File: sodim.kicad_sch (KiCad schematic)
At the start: 7 parts, among them J1 Edge_Conn_Bus_DDR5_SODIMM_1xD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, U7 AT24CS01_SOT23

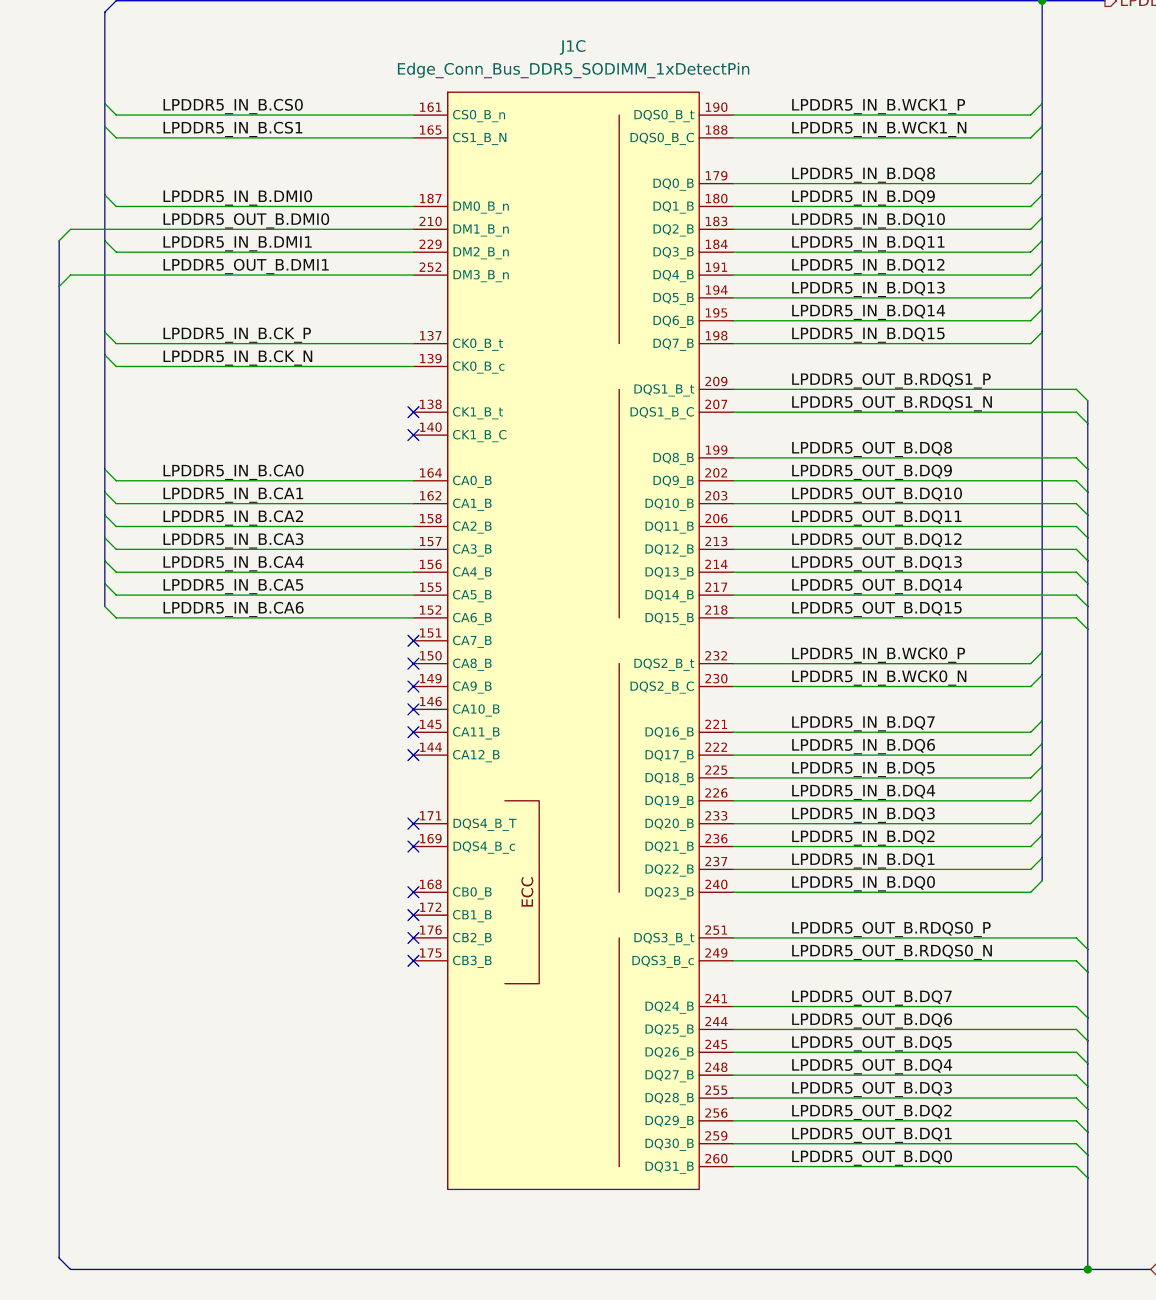
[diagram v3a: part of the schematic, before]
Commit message: [#52835] schematics: swap pins within groups
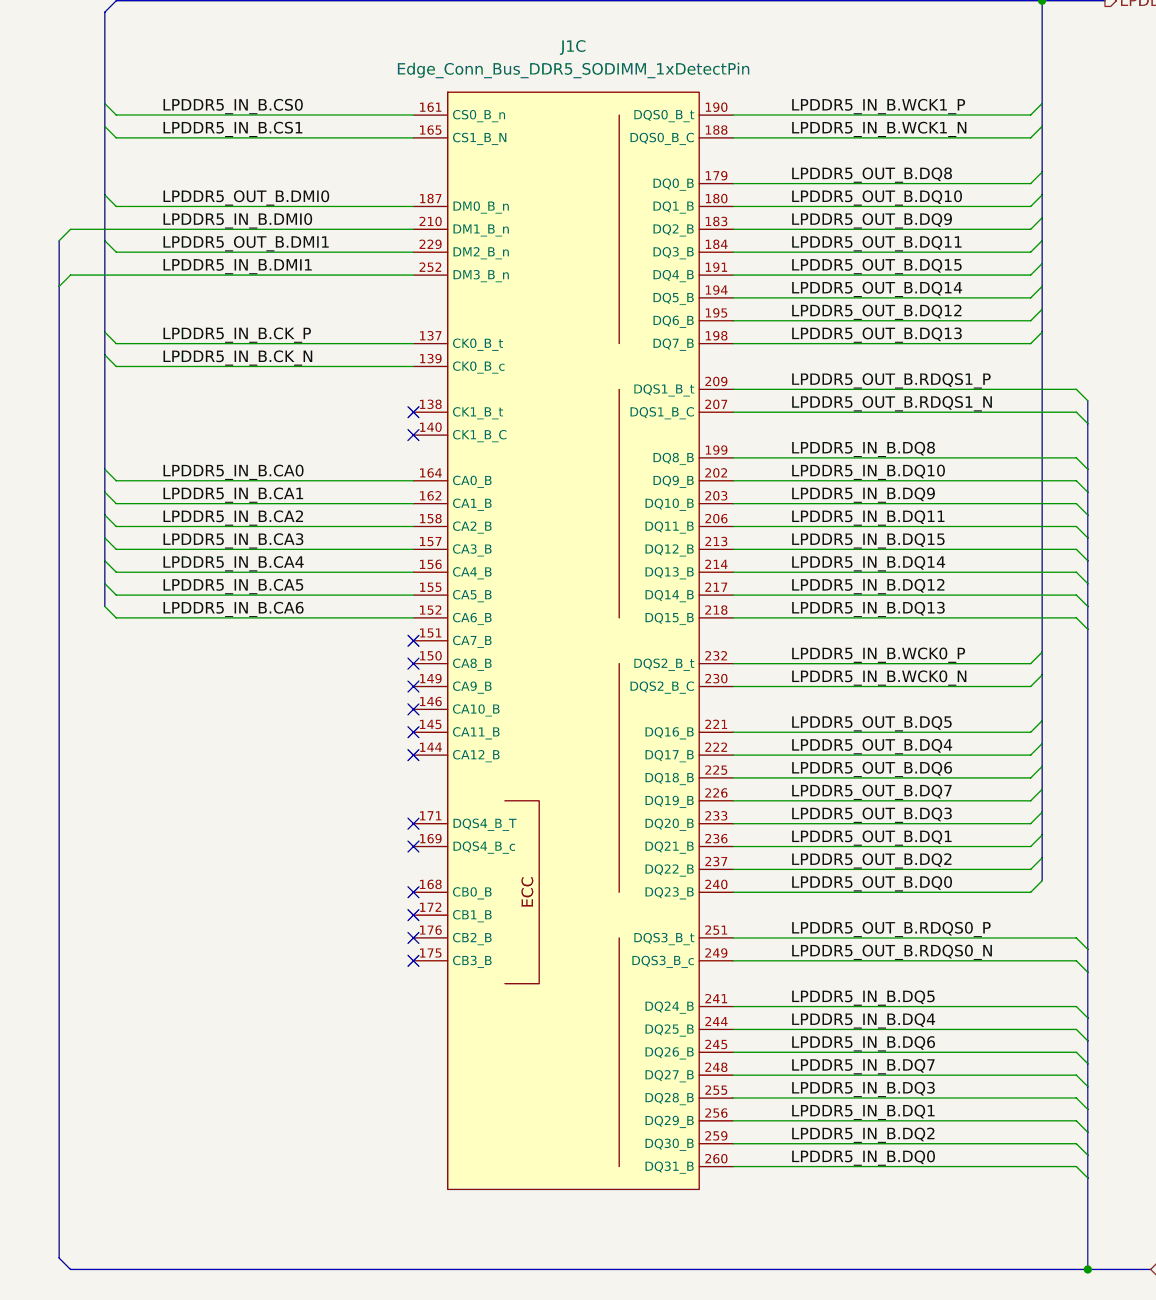
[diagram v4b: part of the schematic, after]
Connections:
- net LPDDR5_IN_B.DMI0: now also J1.210 (DM1_B_n); no longer J1.187 (DM0_B_n)
- net LPDDR5_IN_B.DMI1: now also J1.252 (DM3_B_n); no longer J1.229 (DM2_B_n)
- net LPDDR5_IN_B.DQ0: now also J1.260 (DQ31_B); no longer J1.240 (DQ23_B)
- net LPDDR5_IN_B.DQ1: now also J1.256 (DQ29_B); no longer J1.237 (DQ22_B)
- net LPDDR5_IN_B.DQ10: now also J1.202 (DQ9_B); no longer J1.183 (DQ2_B)
- net LPDDR5_IN_B.DQ11: now also J1.206 (DQ11_B); no longer J1.184 (DQ3_B)
- net LPDDR5_IN_B.DQ12: now also J1.217 (DQ14_B); no longer J1.191 (DQ4_B)
- net LPDDR5_IN_B.DQ13: now also J1.218 (DQ15_B); no longer J1.194 (DQ5_B)
- net LPDDR5_IN_B.DQ14: now also J1.214 (DQ13_B); no longer J1.195 (DQ6_B)
- net LPDDR5_IN_B.DQ15: now also J1.213 (DQ12_B); no longer J1.198 (DQ7_B)
- net LPDDR5_IN_B.DQ2: now also J1.259 (DQ30_B); no longer J1.236 (DQ21_B)
- net LPDDR5_IN_B.DQ3: now also J1.255 (DQ28_B); no longer J1.233 (DQ20_B)
- net LPDDR5_IN_B.DQ4: now also J1.244 (DQ25_B); no longer J1.226 (DQ19_B)
- net LPDDR5_IN_B.DQ5: now also J1.241 (DQ24_B); no longer J1.225 (DQ18_B)
- net LPDDR5_IN_B.DQ6: now also J1.245 (DQ26_B); no longer J1.222 (DQ17_B)
- net LPDDR5_IN_B.DQ7: now also J1.248 (DQ27_B); no longer J1.221 (DQ16_B)
- net LPDDR5_IN_B.DQ8: now also J1.199 (DQ8_B); no longer J1.179 (DQ0_B)
- net LPDDR5_IN_B.DQ9: now also J1.203 (DQ10_B); no longer J1.180 (DQ1_B)
- net LPDDR5_OUT_B.DMI0: now also J1.187 (DM0_B_n); no longer J1.210 (DM1_B_n)
- net LPDDR5_OUT_B.DMI1: now also J1.229 (DM2_B_n); no longer J1.252 (DM3_B_n)
- net LPDDR5_OUT_B.DQ0: now also J1.240 (DQ23_B); no longer J1.260 (DQ31_B)
- net LPDDR5_OUT_B.DQ1: now also J1.236 (DQ21_B); no longer J1.259 (DQ30_B)
- net LPDDR5_OUT_B.DQ10: now also J1.180 (DQ1_B); no longer J1.203 (DQ10_B)
- net LPDDR5_OUT_B.DQ11: now also J1.184 (DQ3_B); no longer J1.206 (DQ11_B)
- net LPDDR5_OUT_B.DQ12: now also J1.195 (DQ6_B); no longer J1.213 (DQ12_B)
- net LPDDR5_OUT_B.DQ13: now also J1.198 (DQ7_B); no longer J1.214 (DQ13_B)
- net LPDDR5_OUT_B.DQ14: now also J1.194 (DQ5_B); no longer J1.217 (DQ14_B)
- net LPDDR5_OUT_B.DQ15: now also J1.191 (DQ4_B); no longer J1.218 (DQ15_B)
- net LPDDR5_OUT_B.DQ2: now also J1.237 (DQ22_B); no longer J1.256 (DQ29_B)
- net LPDDR5_OUT_B.DQ3: now also J1.233 (DQ20_B); no longer J1.255 (DQ28_B)
- net LPDDR5_OUT_B.DQ4: now also J1.222 (DQ17_B); no longer J1.248 (DQ27_B)
- net LPDDR5_OUT_B.DQ5: now also J1.221 (DQ16_B); no longer J1.245 (DQ26_B)
- net LPDDR5_OUT_B.DQ6: now also J1.225 (DQ18_B); no longer J1.244 (DQ25_B)
- net LPDDR5_OUT_B.DQ7: now also J1.226 (DQ19_B); no longer J1.241 (DQ24_B)
- net LPDDR5_OUT_B.DQ8: now also J1.179 (DQ0_B); no longer J1.199 (DQ8_B)
- net LPDDR5_OUT_B.DQ9: now also J1.183 (DQ2_B); no longer J1.202 (DQ9_B)
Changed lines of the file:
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@@
     (effects (font (size 1.27 1.27)) (justify left bottom))
   )
-  (label "LPDDR5_IN_B.DQ3" (at 279.4 182.88 0)
+  (label "LPDDR5_IN_B.DQ3" (at 279.4 213.36 0)
     (effects (font (size 1.27 1.27)) (justify left bottom))
   )
@@
     (effects (font (size 1.27 1.27)) (justify left bottom))
   )
-  (label "LPDDR5_OUT_B.DQ3" (at 279.4 213.36 0)
-    (effects (font (size 1.27 1.27)) (justify left bottom))
-  )
-  (label "LPDDR5_OUT_B.DQ6" (at 279.4 205.74 0)
+  (label "LPDDR5_OUT_B.DQ3" (at 279.4 182.88 0)
+    (effects (font (size 1.27 1.27)) (justify left bottom))
+  )
+  (label "LPDDR5_OUT_B.DQ6" (at 279.4 177.8 0)
     (effects (font (size 1.27 1.27)) (justify left bottom))
   )
@@
     (effects (font (size 1.27 1.27)) (justify left bottom))
   )
-  (label "LPDDR5_IN_B.DQ6" (at 279.4 175.26 0)
+  (label "LPDDR5_IN_B.DQ6" (at 279.4 208.28 0)
     (effects (font (size 1.27 1.27)) (justify left bottom))
   )
@@
     (effects (font (size 1.27 1.27)) (justify left bottom))
   )
-  (label "LPDDR5_IN_B.DMI0" (at 209.55 114.3 0)
-    (effects (font (size 1.27 1.27)) (justify left bottom))
-  )
-  (label "LPDDR5_OUT_B.DQ9" (at 279.4 144.78 0)
+  (label "LPDDR5_IN_B.DMI0" (at 209.55 116.84 0)
+    (effects (font (size 1.27 1.27)) (justify left bottom))
+  )
+  (label "LPDDR5_OUT_B.DQ9" (at 279.4 116.84 0)
     (effects (font (size 1.27 1.27)) (justify left bottom))
   )
@@
     (effects (font (size 1.27 1.27)) (justify left bottom))
   )
-  (label "LPDDR5_IN_B.DQ15" (at 279.4 129.54 0)
+  (label "LPDDR5_IN_B.DQ15" (at 279.4 152.4 0)
     (effects (font (size 1.27 1.27)) (justify left bottom))
   )
@@
     (effects (font (size 1.27 1.27)) (justify left bottom))
   )
-  (label "LPDDR5_OUT_B.DQ14" (at 279.4 157.48 0)
+  (label "LPDDR5_OUT_B.DQ14" (at 279.4 124.46 0)
     (effects (font (size 1.27 1.27)) (justify left bottom))
   )
@@
     (effects (font (size 1.27 1.27)) (justify left bottom))
   )
-  (label "LPDDR5_OUT_B.DQ13" (at 279.4 154.94 0)
-    (effects (font (size 1.27 1.27)) (justify left bottom))
-  )
-  (label "LPDDR5_OUT_B.DQ11" (at 279.4 149.86 0)
-    (effects (font (size 1.27 1.27)) (justify left bottom))
-  )
-  (label "LPDDR5_IN_B.DQ7" (at 279.4 172.72 0)
+  (label "LPDDR5_OUT_B.DQ13" (at 279.4 129.54 0)
+    (effects (font (size 1.27 1.27)) (justify left bottom))
+  )
+  (label "LPDDR5_OUT_B.DQ11" (at 279.4 119.38 0)
+    (effects (font (size 1.27 1.27)) (justify left bottom))
+  )
+  (label "LPDDR5_IN_B.DQ7" (at 279.4 210.82 0)
     (effects (font (size 1.27 1.27)) (justify left bottom))
   )
@@
     (effects (font (size 1.27 1.27)) (justify left bottom))
   )
-  (label "LPDDR5_OUT_B.DMI0" (at 209.55 116.84 0)
-    (effects (font (size 1.27 1.27)) (justify left bottom))
-  )
-  (label "LPDDR5_OUT_B.DQ5" (at 279.4 208.28 0)
+  (label "LPDDR5_OUT_B.DMI0" (at 209.55 114.3 0)
+    (effects (font (size 1.27 1.27)) (justify left bottom))
+  )
+  (label "LPDDR5_OUT_B.DQ5" (at 279.4 172.72 0)
     (effects (font (size 1.27 1.27)) (justify left bottom))
   )
@@
     (effects (font (size 1.27 1.27)) (justify left bottom))
   )
-  (label "LPDDR5_IN_B.DQ5" (at 279.4 177.8 0)
+  (label "LPDDR5_IN_B.DQ5" (at 279.4 203.2 0)
     (effects (font (size 1.27 1.27)) (justify left bottom))
   )
@@
     (effects (font (size 1.27 1.27)) (justify left bottom))
   )
-  (label "LPDDR5_OUT_B.DQ8" (at 279.4 142.24 0)
+  (label "LPDDR5_OUT_B.DQ8" (at 279.4 111.76 0)
     (effects (font (size 1.27 1.27)) (justify left bottom))
   )
@@
     (effects (font (size 1.27 1.27)) (justify left bottom))
   )
-  (label "LPDDR5_OUT_B.DQ10" (at 279.4 147.32 0)
+  (label "LPDDR5_OUT_B.DQ10" (at 279.4 114.3 0)
     (effects (font (size 1.27 1.27)) (justify left bottom))
   )
@@
     (effects (font (size 1.27 1.27)) (justify left bottom))
   )
-  (label "LPDDR5_OUT_B.DQ12" (at 279.4 152.4 0)
+  (label "LPDDR5_OUT_B.DQ12" (at 279.4 127 0)
     (effects (font (size 1.27 1.27)) (justify left bottom))
   )
@@
     (effects (font (size 1.27 1.27)) (justify left bottom))
   )
-  (label "LPDDR5_IN_B.DQ8" (at 279.4 111.76 0)
+  (label "LPDDR5_IN_B.DQ8" (at 279.4 142.24 0)
     (effects (font (size 1.27 1.27)) (justify left bottom))
   )
@@
     (effects (font (size 1.27 1.27)) (justify left bottom))
   )
-  (label "LPDDR5_OUT_B.DQ1" (at 279.4 218.44 0)
-    (effects (font (size 1.27 1.27)) (justify left bottom))
-  )
-  (label "LPDDR5_IN_B.DMI1" (at 209.55 119.38 0)
+  (label "LPDDR5_OUT_B.DQ1" (at 279.4 185.42 0)
+    (effects (font (size 1.27 1.27)) (justify left bottom))
+  )
+  (label "LPDDR5_IN_B.DMI1" (at 209.55 121.92 0)
     (effects (font (size 1.27 1.27)) (justify left bottom))
   )
@@
     (effects (font (size 1.27 1.27)) (justify left bottom))
   )
-  (label "LPDDR5_OUT_B.DMI1" (at 209.55 121.92 0)
+  (label "LPDDR5_OUT_B.DMI1" (at 209.55 119.38 0)
     (effects (font (size 1.27 1.27)) (justify left bottom))
   )
@@
     (effects (font (size 1.27 1.27)) (justify left bottom))
   )
-  (label "LPDDR5_IN_B.DQ4" (at 279.4 180.34 0)
+  (label "LPDDR5_IN_B.DQ4" (at 279.4 205.74 0)
     (effects (font (size 1.27 1.27)) (justify left bottom))
   )
@@
     (effects (font (size 1.27 1.27)) (justify left bottom))
   )
-  (label "LPDDR5_IN_B.DQ9" (at 279.4 114.3 0)
+  (label "LPDDR5_IN_B.DQ9" (at 279.4 147.32 0)
     (effects (font (size 1.27 1.27)) (justify left bottom))
   )
@@
     (effects (font (size 1.27 1.27)) (justify left bottom))
   )
-  (label "LPDDR5_OUT_B.DQ0" (at 279.4 220.98 0)
-    (effects (font (size 1.27 1.27)) (justify left bottom))
-  )
-  (label "LPDDR5_IN_B.DQ2" (at 279.4 185.42 0)
+  (label "LPDDR5_OUT_B.DQ0" (at 279.4 190.5 0)
+    (effects (font (size 1.27 1.27)) (justify left bottom))
+  )
+  (label "LPDDR5_IN_B.DQ2" (at 279.4 218.44 0)
     (effects (font (size 1.27 1.27)) (justify left bottom))
   )
@@
     (effects (font (size 1.27 1.27)) (justify left bottom))
   )
-  (label "LPDDR5_IN_B.DQ10" (at 279.4 116.84 0)
-    (effects (font (size 1.27 1.27)) (justify left bottom))
-  )
-  (label "LPDDR5_IN_B.DQ1" (at 279.4 187.96 0)
+  (label "LPDDR5_IN_B.DQ10" (at 279.4 144.78 0)
+    (effects (font (size 1.27 1.27)) (justify left bottom))
+  )
+  (label "LPDDR5_IN_B.DQ1" (at 279.4 215.9 0)
     (effects (font (size 1.27 1.27)) (justify left bottom))
   )
@@
     (effects (font (size 1.27 1.27)) (justify left bottom))
   )
-  (label "LPDDR5_IN_B.DQ11" (at 279.4 119.38 0)
+  (label "LPDDR5_IN_B.DQ11" (at 279.4 149.86 0)
     (effects (font (size 1.27 1.27)) (justify left bottom))
   )
@@
     (effects (font (size 1.27 1.27)) (justify left bottom))
   )
-  (label "LPDDR5_OUT_B.DQ15" (at 279.4 160.02 0)
-    (effects (font (size 1.27 1.27)) (justify left bottom))
-  )
-  (label "LPDDR5_OUT_B.DQ7" (at 279.4 203.2 0)
+  (label "LPDDR5_OUT_B.DQ15" (at 279.4 121.92 0)
+    (effects (font (size 1.27 1.27)) (justify left bottom))
+  )
+  (label "LPDDR5_OUT_B.DQ7" (at 279.4 180.34 0)
     (effects (font (size 1.27 1.27)) (justify left bottom))
   )
@@
     (effects (font (size 1.27 1.27)) (justify left bottom))
   )
-  (label "LPDDR5_IN_B.DQ14" (at 279.4 127 0)
-    (effects (font (size 1.27 1.27)) (justify left bottom))
-  )
-  (label "LPDDR5_OUT_B.DQ2" (at 279.4 215.9 0)
-    (effects (font (size 1.27 1.27)) (justify left bottom))
-  )
-  (label "LPDDR5_OUT_B.DQ4" (at 279.4 210.82 0)
+  (label "LPDDR5_IN_B.DQ14" (at 279.4 154.94 0)
+    (effects (font (size 1.27 1.27)) (justify left bottom))
+  )
+  (label "LPDDR5_OUT_B.DQ2" (at 279.4 187.96 0)
+    (effects (font (size 1.27 1.27)) (justify left bottom))
+  )
+  (label "LPDDR5_OUT_B.DQ4" (at 279.4 175.26 0)
     (effects (font (size 1.27 1.27)) (justify left bottom))
   )
@@
     (effects (font (size 1.27 1.27)) (justify left bottom))
   )
-  (label "LPDDR5_IN_B.DQ13" (at 279.4 124.46 0)
+  (label "LPDDR5_IN_B.DQ13" (at 279.4 160.02 0)
     (effects (font (size 1.27 1.27)) (justify left bottom))
   )
@@
     (effects (font (size 1.27 1.27)) (justify left bottom))
   )
-  (label "LPDDR5_IN_B.DQ0" (at 279.4 190.5 0)
+  (label "LPDDR5_IN_B.DQ0" (at 279.4 220.98 0)
     (effects (font (size 1.27 1.27)) (justify left bottom))
   )
@@
     (effects (font (size 1.27 1.27)) (justify left bottom))
   )
-  (label "LPDDR5_IN_B.DQ12" (at 279.4 121.92 0)
-    (effects (font (size 1.27 1.27)) (justify left bottom))
-  )
+  (label "LPDDR5_IN_B.DQ12" (at 279.4 157.48 0)
+    (effects (font (size 1.27 1.27)) (justify left bottom))
+  )

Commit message: [#52835] update project name
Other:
- note removed: "0"
- note removed: "1"
- note removed: "CA[5:0]"
- note removed: "DMI_A0"
- note removed: "DMI_A0_DIR"
- note removed: "DMI_A1"
- note removed: "DQL_DIR"
- note removed: "DQ[7:0]"
- note removed: "FPGA -> MEM"
- note removed: "MEM -> FPGA"
- note removed: "RDQS_A_0"
- note removed: "RDQS_A_1"
- note removed: "WCK, CS, CK_A, WCK_A"
- note removed: "~{RESET}"
- title: LPDDR5 SO-DIMM -> LPDDR5 Testbed

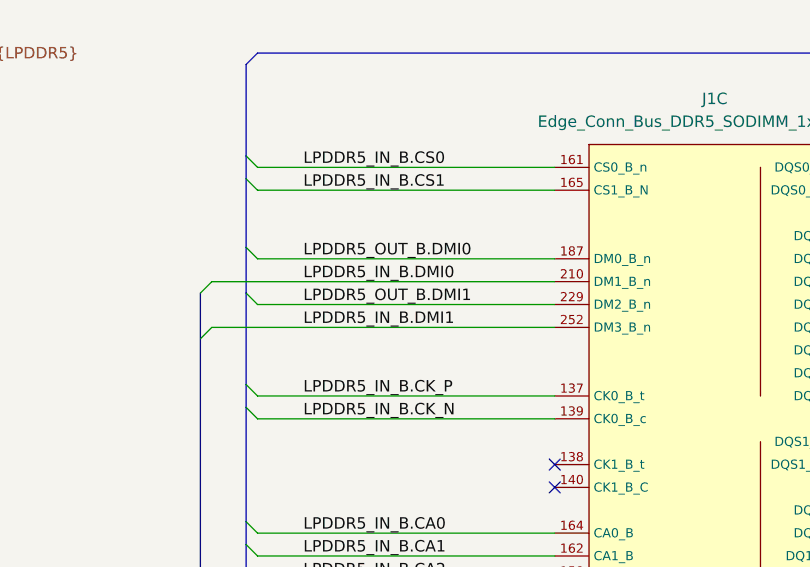
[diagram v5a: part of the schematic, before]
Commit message: [#52835] schematics: swap DMI pins on side B
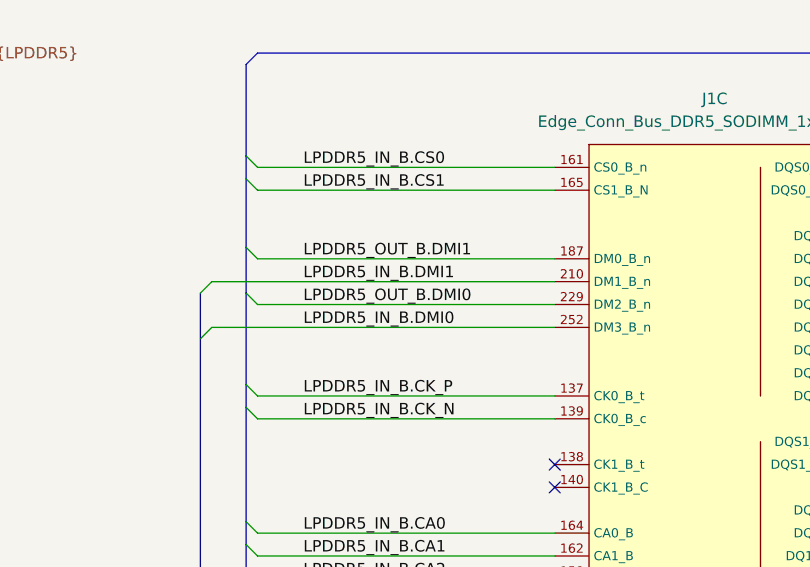
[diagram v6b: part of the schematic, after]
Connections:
- net LPDDR5_IN_B.DMI0: now also J1.252 (DM3_B_n); no longer J1.210 (DM1_B_n)
- net LPDDR5_IN_B.DMI1: now also J1.210 (DM1_B_n); no longer J1.252 (DM3_B_n)
- net LPDDR5_OUT_B.DMI0: now also J1.229 (DM2_B_n); no longer J1.187 (DM0_B_n)
- net LPDDR5_OUT_B.DMI1: now also J1.187 (DM0_B_n); no longer J1.229 (DM2_B_n)
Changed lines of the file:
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@@
     (effects (font (size 1.27 1.27)) (justify left bottom))
   )
-  (label "LPDDR5_IN_B.DMI0" (at 209.55 116.84 0)
+  (label "LPDDR5_IN_B.DMI0" (at 209.55 121.92 0)
     (effects (font (size 1.27 1.27)) (justify left bottom))
   )
@@
     (effects (font (size 1.27 1.27)) (justify left bottom))
   )
-  (label "LPDDR5_OUT_B.DMI0" (at 209.55 114.3 0)
+  (label "LPDDR5_OUT_B.DMI0" (at 209.55 119.38 0)
     (effects (font (size 1.27 1.27)) (justify left bottom))
   )
@@
     (effects (font (size 1.27 1.27)) (justify left bottom))
   )
-  (label "LPDDR5_IN_B.DMI1" (at 209.55 121.92 0)
+  (label "LPDDR5_IN_B.DMI1" (at 209.55 116.84 0)
     (effects (font (size 1.27 1.27)) (justify left bottom))
   )
@@
     (effects (font (size 1.27 1.27)) (justify left bottom))
   )
-  (label "LPDDR5_OUT_B.DMI1" (at 209.55 119.38 0)
+  (label "LPDDR5_OUT_B.DMI1" (at 209.55 114.3 0)
     (effects (font (size 1.27 1.27)) (justify left bottom))
   )
